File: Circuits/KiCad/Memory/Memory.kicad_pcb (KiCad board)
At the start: 2 copper layers, 27 parts, among them J1 Conn_01x13_Male, J2 Conn_01x16_Male, SW1 SW_DPDT_x2, SW10 SW_DPDT_x2, SW2 SW_DPDT_x2, SW3 SW_DPDT_x2, SW4 SW_DPDT_x2, SW5 SW_DPDT_x2, SW6 SW_DPDT_x2, SW7 SW_DPDT_x2, SW8 SW_DPDT_x2, SW9 SW_DPDT_x2, U1 74x04, U2 74x00, U3 74x02, U4 74x32, U5 UM61512AK-15, U6 27C512, U7 74x245, U8 74x245, U9 74x245

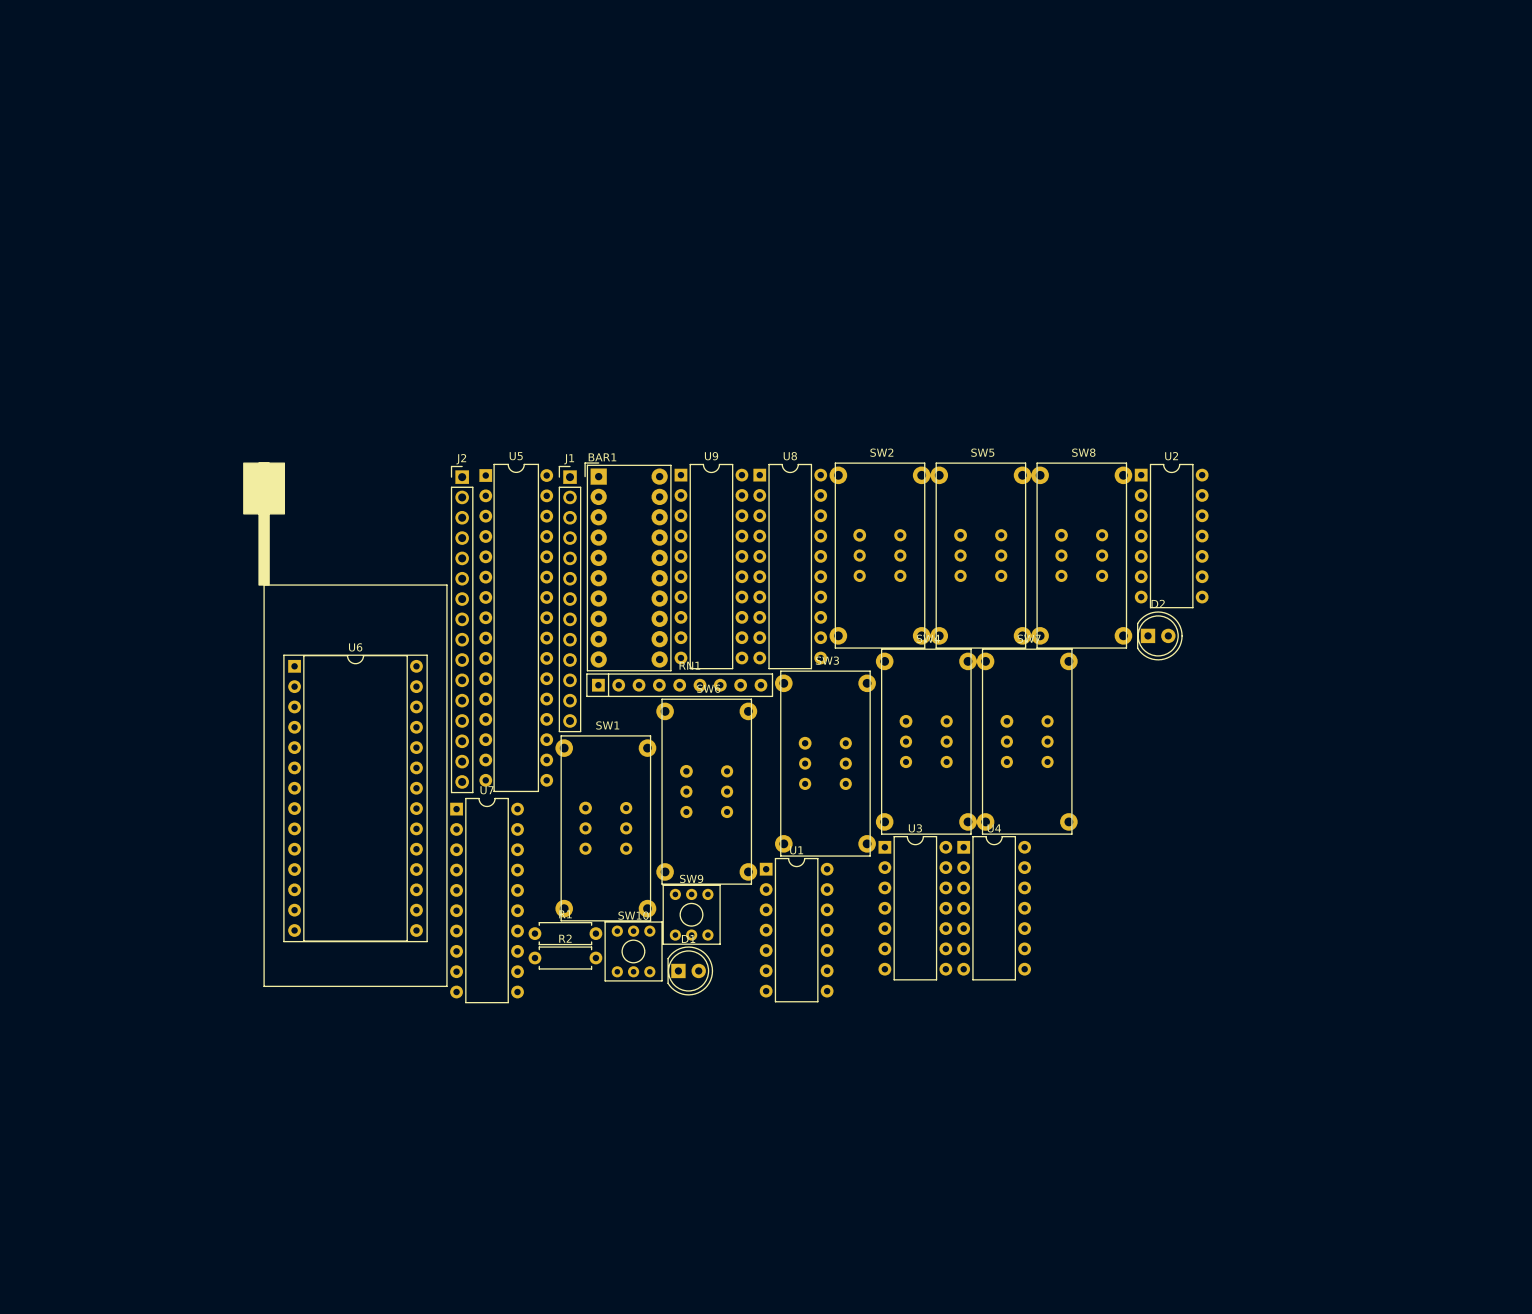
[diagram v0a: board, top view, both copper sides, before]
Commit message: Routed MAR PCB
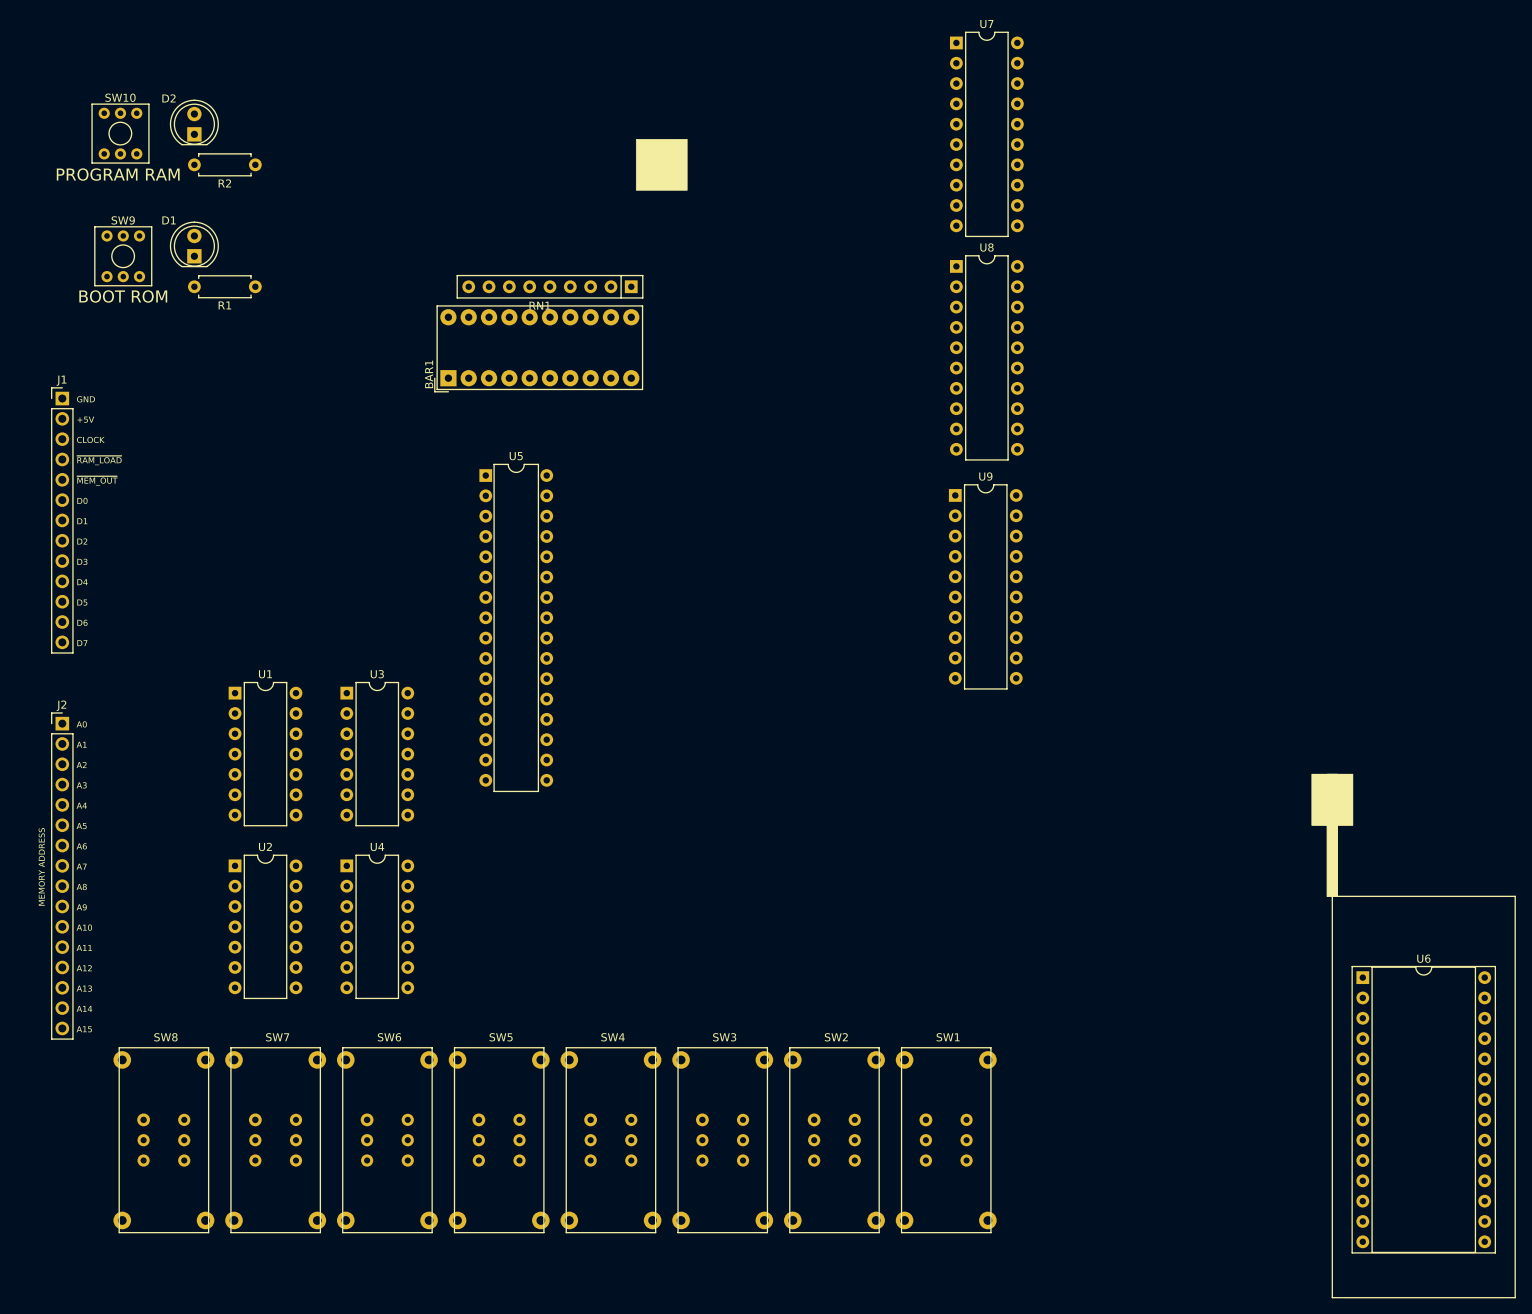
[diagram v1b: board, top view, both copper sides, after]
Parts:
- moved U6 139.1 mm to (191.8, 101.6)
- moved SW8 136.0 mm to (41.9, 121.9)
- moved D2 134.7 mm to (45.7, -3.81), turned to 90 degrees
- moved U2 123.4 mm to (50.8, 87.6)
- moved SW10 120.7 mm to (36.5, -3.91)
- moved U7 114.4 mm to (141.0, -15.2)
- moved SW9 108.7 mm to (36.8, 11.4)
- moved D1 107.9 mm to (45.7, 11.4), turned to 90 degrees
- moved SW7 106.3 mm to (55.9, 121.9)
- moved R2 105.1 mm to (53.3, 0.00), turned to 180 degrees
- moved SW5 94.7 mm to (83.8, 121.9)
- moved R1 88.1 mm to (53.3, 15.2), turned to 180 degrees
- moved U4 77.1 mm to (64.8, 87.6)
- moved SW2 73.3 mm to (125.7, 121.9)
- moved U3 70.0 mm to (64.8, 66.0)
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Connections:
- U1 pad 14: (no net) -> +5V
- U1 pad 7: (no net) -> GND
- U2 pad 14: (no net) -> +5V
- U2 pad 7: (no net) -> GND
- U3 pad 14: (no net) -> +5V
- U3 pad 7: (no net) -> GND
- U4 pad 14: (no net) -> +5V
- U4 pad 7: (no net) -> GND
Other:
- board text added: "+5V"
- board text added: "A0"
- board text added: "A1"
- board text added: "A10"
- board text added: "A11"
- board text added: "A12"
- board text added: "A13"
- board text added: "A14"
- board text added: "A15"
- board text added: "A2"
- board text added: "A3"
- board text added: "A4"
- board text added: "A5"
- board text added: "A6"
- board text added: "A7"
- board text added: "A8"
- board text added: "A9"
- board text added: "BOOT ROM"
- board text added: "CLOCK"
- board text added: "D0"
- board text added: "D1"
- board text added: "D2"
- board text added: "D3"
- board text added: "D4"
- board text added: "D5"
- board text added: "D6"
- board text added: "D7"
- board text added: "GND"
- board text added: "MEMORY ADDRESS"
- board text added: "PROGRAM RAM"
- board text added: "~MEM_OUT"
- board text added: "~RAM_LOAD"

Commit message: Finished Memory & Memory Access Register PCB
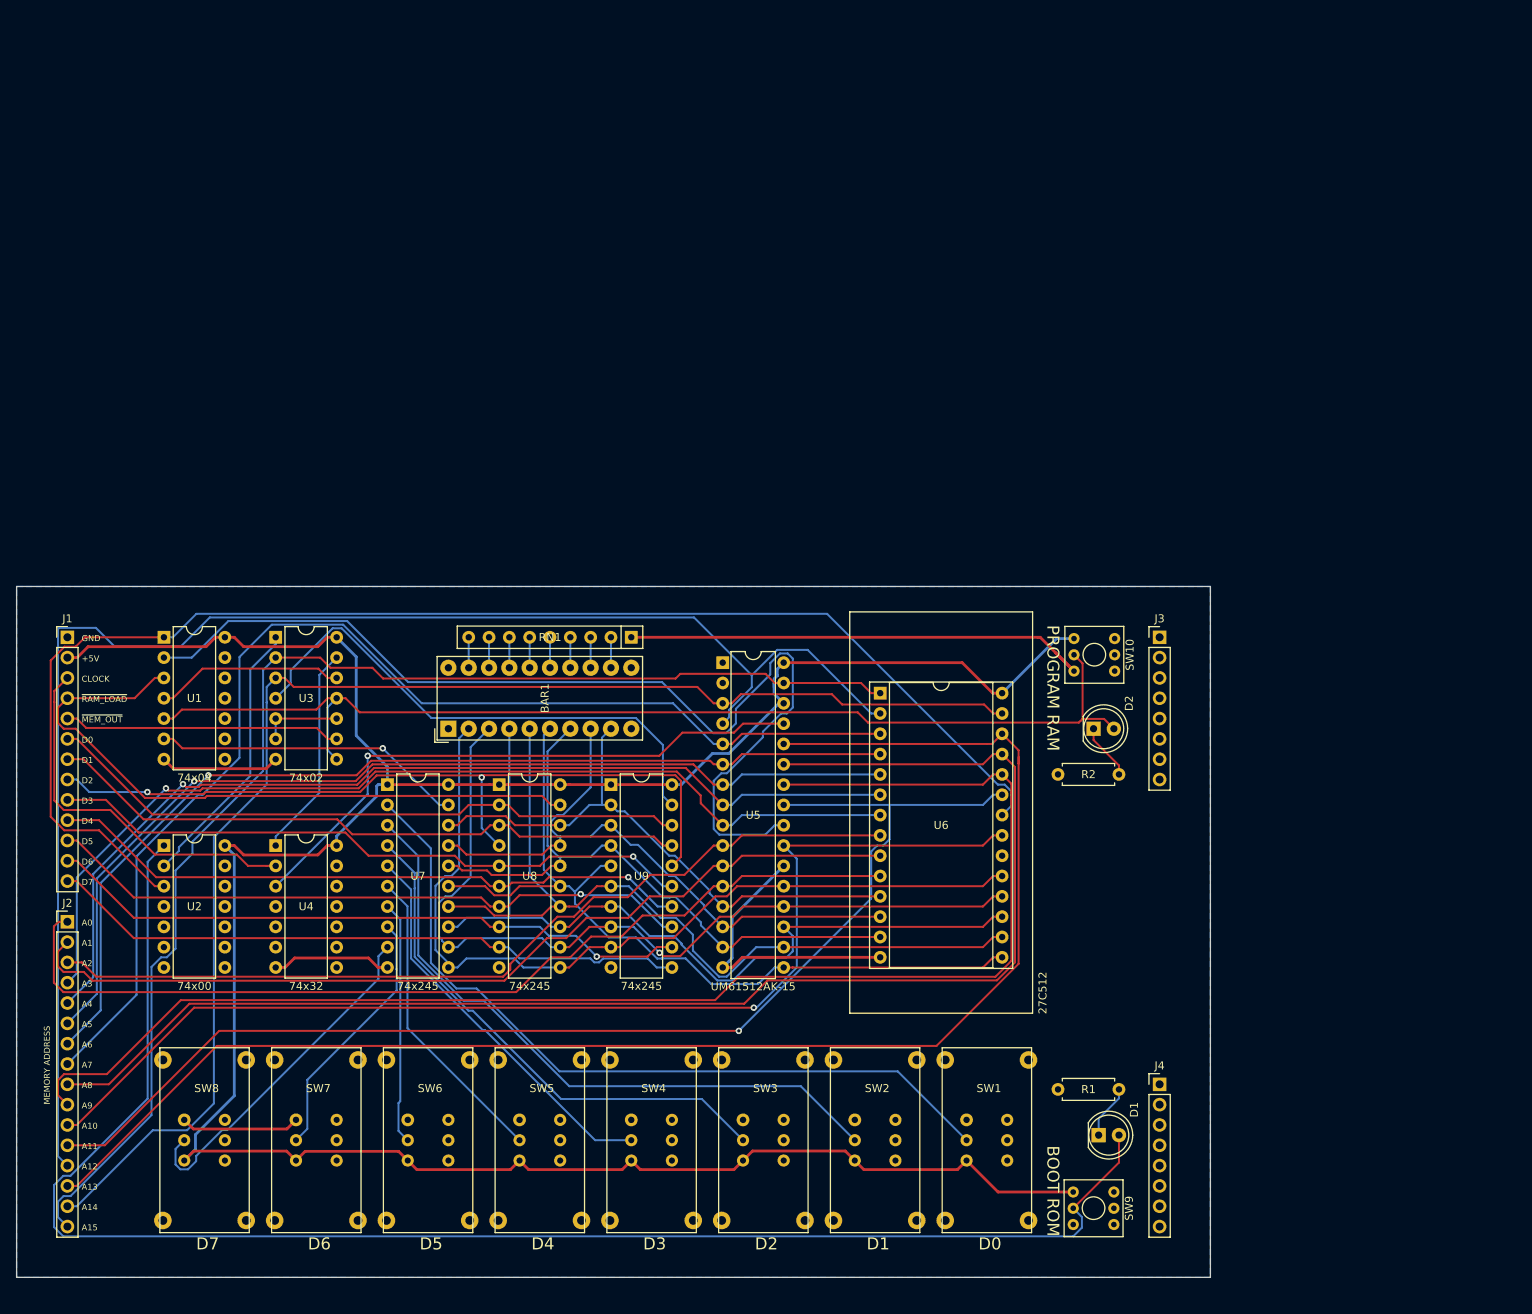
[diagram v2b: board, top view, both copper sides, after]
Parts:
- added J3: Conn_01x08_Male, Connector_PinHeader_2.54mm:PinHeader_1x08_P2.54mm_Vertical, F.Cu at (166.4, 59.1)
- added J4: Conn_01x08_Male, Connector_PinHeader_2.54mm:PinHeader_1x08_P2.54mm_Vertical, F.Cu at (166.4, 114.9)
- moved SW9 169.9 mm to (158.1, 130.4), turned to 270 degrees
- moved D1 157.6 mm to (158.8, 121.3), turned to 0 degrees
- moved R1 141.9 mm to (153.7, 115.6), turned to 0 degrees
- moved SW10 138.1 mm to (158.2, 61.2), turned to 270 degrees
- moved D2 134.7 mm to (158.1, 70.5), turned to 0 degrees
- moved R2 126.0 mm to (153.7, 76.2), turned to 0 degrees
- moved U7 116.8 mm to (69.8, 77.5)
- moved U8 86.4 mm to (83.8, 77.5)
- moved U6 70.0 mm to (131.4, 66.0)
- moved U9 56.2 mm to (97.8, 77.5)
- moved BAR1 43.8 mm to (77.5, 70.5)
- moved RN1 43.8 mm to (100.3, 59.1)
- moved U5 37.7 mm to (111.8, 62.2)
- moved J1 29.9 mm to (29.8, 59.1)
- moved J2 24.8 mm to (29.8, 94.6)
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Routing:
- net +5V: track 0.00 -> 346.3 mm
- net BOOT_ROM: track 0.00 -> 197.7 mm
- net Net-(J2-Pad14): track 0.00 -> 188.6 mm
- net Net-(J2-Pad13): track 0.00 -> 188.0 mm
- net Net-(J2-Pad10): track 0.00 -> 180.5 mm
- net Net-(J2-Pad9): track 0.00 -> 179.3 mm
- net Net-(J2-Pad15): track 0.00 -> 173.6 mm
- net ~ROM_OE: track 0.00 -> 172.4 mm
- net Net-(J2-Pad16): track 0.00 -> 161.7 mm
- net Net-(J2-Pad12): track 0.00 -> 154.2 mm, vias 0 -> 1
- net Net-(J2-Pad8): track 0.00 -> 148.6 mm
- net Net-(J2-Pad11): track 0.00 -> 143.1 mm, vias 0 -> 1
- net GND: track 0.00 -> 141.3 mm
- net PROGRAM_RAM: track 0.00 -> 138.8 mm
- net ~RAM_OE: track 0.00 -> 128.4 mm
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- added copper zone on B.Cu, net GND
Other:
- board outline added: 149.2 x 86.4 mm
- net class Power added: clearance 0.2, trace_width 0.35, via_dia 0.8, via_drill 0.4
